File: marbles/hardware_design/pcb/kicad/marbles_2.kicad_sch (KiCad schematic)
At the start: 28 parts

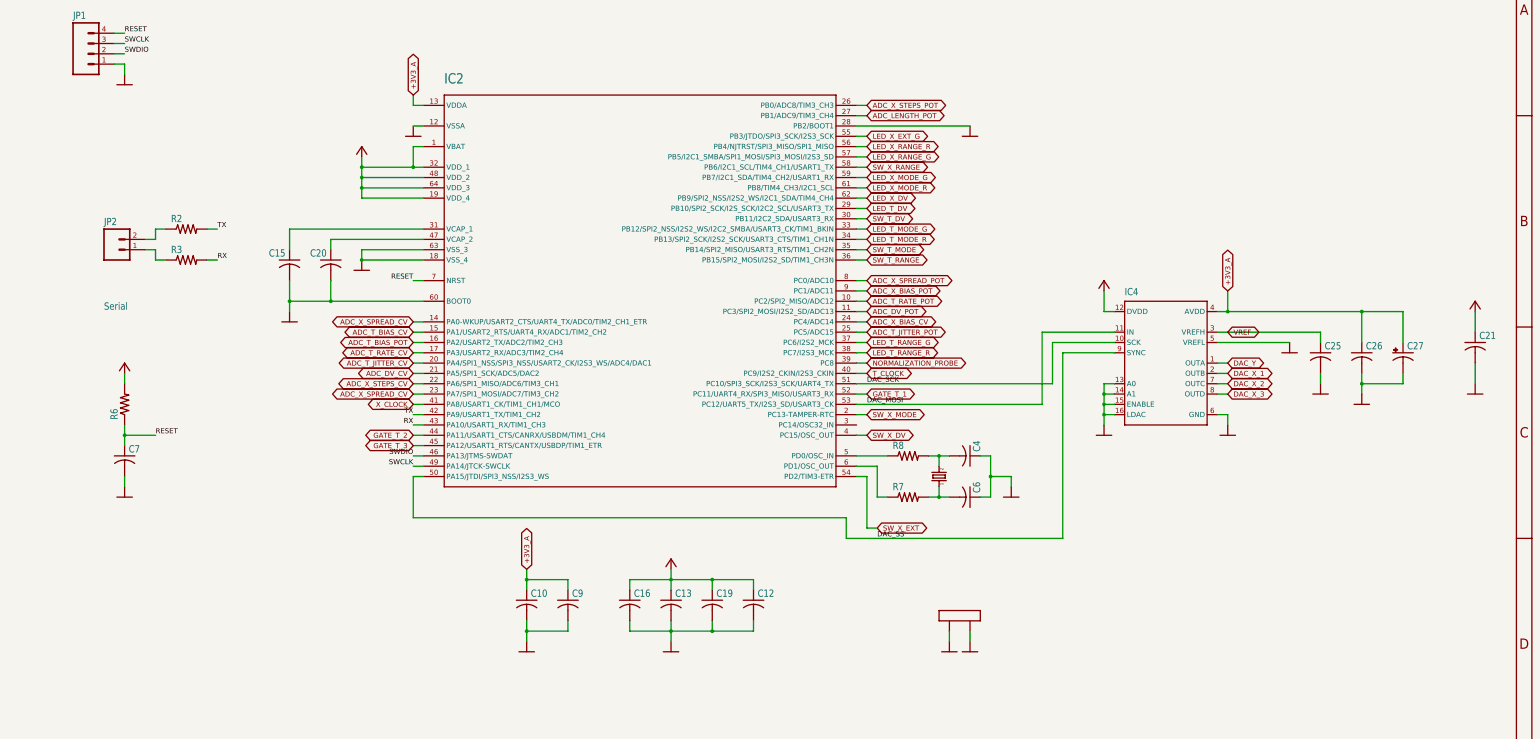
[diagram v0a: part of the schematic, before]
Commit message: added SMD LEDs in parallel with THT footprint
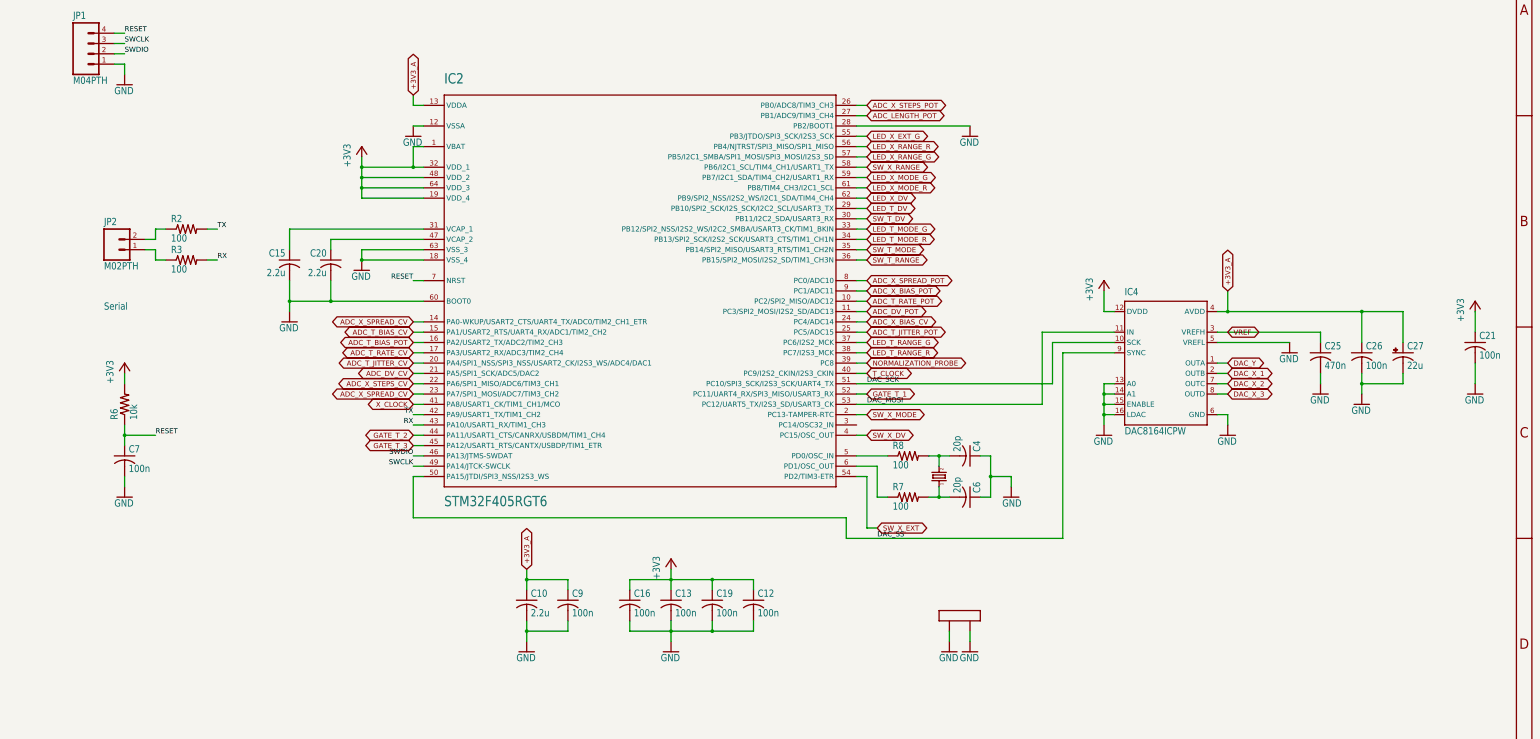
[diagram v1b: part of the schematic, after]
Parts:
- C10, C15, C20: value (none) -> 2.2u; footprint (none) -> marbles:C0805
- C12, C13, C16, C19, C21, C26, C7, C9: value (none) -> 100n; footprint (none) -> marbles:C0402
- C25: value (none) -> 470n; footprint (none) -> marbles:C0402
- C27: value (none) -> 22u; footprint (none) -> marbles:PANASONIC_C
- C4, C6: value (none) -> 20p; footprint (none) -> marbles:C0402
- F1, F2, F3: value (none) -> FIDUCIAL1X2; footprint (none) -> marbles:FIDUCIAL-1X2
- IC2: value (none) -> STM32F405RGT6; footprint (none) -> marbles:TQFP-10X10-64
- IC4: value (none) -> DAC8164ICPW; footprint (none) -> marbles:SOP65P640X110-16N
- JP1: value (none) -> M04PTH; footprint (none) -> marbles:1X04
- JP2: value (none) -> M02PTH; footprint (none) -> marbles:1X02
- Q1: value (none) -> 8MHz; footprint (none) -> marbles:CTS406
- R2, R3, R7, R8: value (none) -> 100; footprint (none) -> marbles:R0402
- R6: value (none) -> 10k; footprint (none) -> marbles:R0402

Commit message: change dac from 8164 to 8565
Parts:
- removed IC4: DAC8164ICPW, marbles:SOP65P640X110-16N, symbol marbles-eagle-import:DAC8564
- added IC4: DAC8565, Package_SO:TSSOP-16_4.4x5mm_P0.65mm, symbol Analog_DAC:DAC8565
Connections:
- net +3V3: now also IC4.12 (IOVDD), IC4.13 (~{RST})
- net +3V3_A: now also IC4.4 (AVDD)
- net DAC_MOSI: now also IC4.11 (DIN)
- net DAC_SCK: now also IC4.10 (SCLK)
- net DAC_SS: now also IC4.9 (~{SYNC})
- net DAC_X_1: now also IC4.2 (VOUTB)
- net DAC_X_2: now also IC4.7 (VOUTC)
- net DAC_X_3: now also IC4.8 (VOUTD)
- net DAC_Y: now also IC4.1 (VOUTA)
- net GND: now also IC4.14 (RSTSEL), IC4.15 (~{ENABLE}), IC4.16 (LDAC), IC4.5 (VREFL), IC4.6 (GND)
- net VREF: now also IC4.3 (VREFH/VREFOUT)
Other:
- moved on the sheet: C25, C26, C27

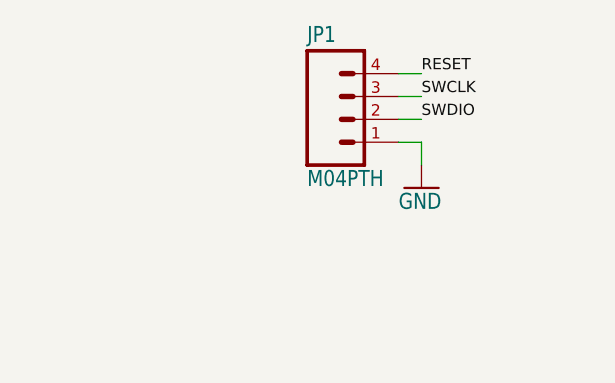
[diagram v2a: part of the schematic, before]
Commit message: add smd flash header in parallel
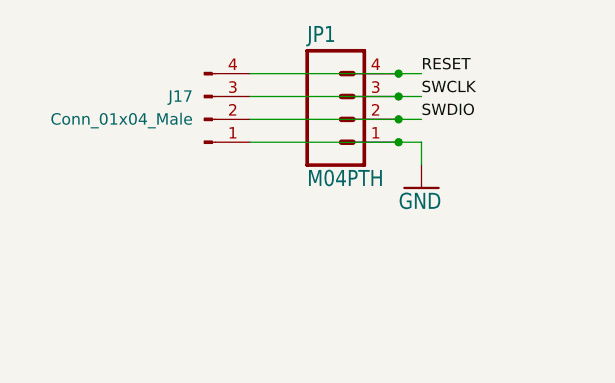
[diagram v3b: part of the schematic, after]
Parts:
- added J17: Conn_01x04_Male, Connector_PinHeader_2.54mm:PinHeader_1x04_P2.54mm_Vertical_SMD_Pin1Left, symbol Connector:Conn_01x04_Male
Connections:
- net GND: now also J17.1 (Pin_1)
- net RESET: now also J17.4 (Pin_4)
- net SWCLK: now also J17.3 (Pin_3)
- net SWDIO: now also J17.2 (Pin_2)
